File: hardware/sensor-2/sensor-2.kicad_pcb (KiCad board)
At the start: 2 copper layers, 11 x 155 mm, 16 parts, among them J101 2x05_Horizontal, U101 A31010SEHALT-10, U102 A31010SEHALT-10, U103 A31010SEHALT-10

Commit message: Update sensors
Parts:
- C101, C103, C104: footprint Capacitor_SMD:C_0603_1608Metric -> V2_Capacitor_SMD:C_0603
- FID101, FID102: value Fiducial -> Fiducial_Paste
- INFO101: value ORDER-NUMBER -> Order_Number

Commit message: Replace Order_Number
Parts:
- H107, H108: value MountingHole_2.5mm -> 2.5mm
- INFO101: value Order_Number -> ~; footprint V2_Production:Order_Number -> V2_Production:Revision
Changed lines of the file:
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@@
 	(paper "A4")
 	(title_block
-		(date "2023-07-17")
-		(rev "1")
+		(date "2026-02-13")
+		(rev "2026-02-13")
 	)
 	(layers
@@
 			)
 		)
+		(pad "" smd roundrect
+			(at -0.7 0)
+			(size 0.7 0.8)
+			(layers "F.Paste")
+			(roundrect_rratio 0.1428571429)
+			(chamfer_ratio 0.3)
+			(chamfer top_right bottom_right)
+		)
+		(pad "" smd roundrect
+			(at 0.7 0)
+			(size 0.7 0.8)
+			(layers "F.Paste")
+			(roundrect_rratio 0.1428571429)
+			(chamfer_ratio 0.3)
+			(chamfer top_left bottom_left)
+		)
 		(pad "1" smd roundrect
 			(at -0.7 0)
 			(size 0.7 0.8)
-			(layers "F.Cu" "F.Mask" "F.Paste")
+			(layers "F.Cu" "F.Mask")
 			(roundrect_rratio 0.1428571429)
 			(net 1 "+3V3")
@@
 			(at 0.7 0)
 			(size 0.7 0.8)
-			(layers "F.Cu" "F.Mask" "F.Paste")
+			(layers "F.Cu" "F.Mask")
 			(roundrect_rratio 0.1428571429)
 			(net 4 "GND")
@@
 		)
 		(embedded_fonts no)
-		(model "${KICAD9_3DMODEL_DIR}/Capacitor_SMD.3dshapes/C_0603_1608Metric.step"
+		(model "../../3dmodels/V2_Capacitor_SMD.3dshapes/C_0603_1608Metric.step"
 			(offset
 				(xyz 0 0 0)
@@
 		)
 		(embedded_fonts no)
-		(model "/Users/kay/Documents/KiCad/8.0/versioduo.kicad/3dmodels/V2_Sensor_Hall.3dshapes/A31010SEHALT-10.stp"
+		(model "../../3dmodels/V2_Sensor_Hall.3dshapes/A31010SEHALT-10.stp"
 			(offset
 				(xyz 0 0 0)
@@
 			)
 		)
-		(property "Value" "MountingHole_2.5mm"
+		(property "Value" "2.5mm"
 			(at 0 2.23 0)
 			(unlocked yes)
@@
 			)
 		)
+		(pad "" smd roundrect
+			(at -0.7 0)
+			(size 0.7 0.8)
+			(layers "F.Paste")
+			(roundrect_rratio 0.1428571429)
+			(chamfer_ratio 0.3)
+			(chamfer top_right bottom_right)
+		)
+		(pad "" smd roundrect
+			(at 0.7 0)
+			(size 0.7 0.8)
+			(layers "F.Paste")
+			(roundrect_rratio 0.1428571429)
+			(chamfer_ratio 0.3)
+			(chamfer top_left bottom_left)
+		)
 		(pad "1" smd roundrect
 			(at -0.7 0)
 			(size 0.7 0.8)
-			(layers "F.Cu" "F.Mask" "F.Paste")
+			(layers "F.Cu" "F.Mask")
 			(roundrect_rratio 0.1428571429)
 			(net 1 "+3V3")
@@
 			(at 0.7 0)
 			(size 0.7 0.8)
-			(layers "F.Cu" "F.Mask" "F.Paste")
+			(layers "F.Cu" "F.Mask")
 			(roundrect_rratio 0.1428571429)
 			(net 4 "GND")
@@
 		)
 		(embedded_fonts no)
-		(model "${KICAD9_3DMODEL_DIR}/Capacitor_SMD.3dshapes/C_0603_1608Metric.step"
+		(model "../../3dmodels/V2_Capacitor_SMD.3dshapes/C_0603_1608Metric.step"
 			(offset
 				(xyz 0 0 0)
@@
 		)
 		(embedded_fonts no)
-		(model "/Users/kay/Documents/KiCad/8.0/versioduo.kicad/3dmodels/V2_Sensor_Hall.3dshapes/A31010SEHALT-10.stp"
+		(model "../../3dmodels/V2_Sensor_Hall.3dshapes/A31010SEHALT-10.stp"
 			(offset
 				(xyz 0 0 0)
@@
 		)
 	)
-	(footprint "V2_Production:Order_Number"
+	(footprint "V2_Production:Revision"
 		(layer "F.Cu")
 		(at 159.75 78.25 90)
@@
 			)
 		)
-		(property "Value" "Order_Number"
+		(property "Value" "~"
 			(at 0 2.27 90)
 			(unlocked yes)
@@
 		(sheetname "/")
 		(sheetfile "sensor-2.kicad_sch")
-		(attr exclude_from_pos_files exclude_from_bom)
-		(fp_rect
-			(start -7 -0.75)
-			(end 7 0.75)
-			(stroke
-				(width 0.05)
-				(type default)
-			)
-			(fill no)
-			(layer "F.CrtYd")
-		)
-		(fp_text user "${Order-Number}"
+		(attr exclude_from_pos_files exclude_from_bom allow_missing_courtyard)
+		(fp_text user "${REVISION} (${ISSUE_DATE})"
 			(at 0 0 90)
 			(unlocked yes)
@@
 			(effects
 				(font
-					(size 0.8 0.8)
-					(thickness 0.12)
+					(size 0.75 0.75)
+					(thickness 0.1)
+				)
+			)
+		)
+		(fp_text user "${REVISION} (${ISSUE_DATE})"
+			(at 0 0 90)
+			(unlocked yes)
+			(layer "F.Fab")
+			(effects
+				(font
+					(size 0.75 0.75)
+					(thickness 0.1)
 				)
 			)
@@
 		)
 		(embedded_fonts no)
-		(model "/Users/kay/Documents/KiCad/8.0/versioduo.kicad/3dmodels/V2_Sensor_Hall.3dshapes/A31010SEHALT-10.stp"
+		(model "../../3dmodels/V2_Sensor_Hall.3dshapes/A31010SEHALT-10.stp"
 			(offset
 				(xyz 0 0 0)
@@
 			)
 		)
-		(property "Value" "MountingHole_2.5mm"
+		(property "Value" "2.5mm"
 			(at 0 2.23 0)
 			(unlocked yes)
@@
 			)
 		)
+		(pad "" smd roundrect
+			(at -0.7 0)
+			(size 0.7 0.8)
+			(layers "F.Paste")
+			(roundrect_rratio 0.1428571429)
+			(chamfer_ratio 0.3)
+			(chamfer top_right bottom_right)
+		)
+		(pad "" smd roundrect
+			(at 0.7 0)
+			(size 0.7 0.8)
+			(layers "F.Paste")
+			(roundrect_rratio 0.1428571429)
+			(chamfer_ratio 0.3)
+			(chamfer top_left bottom_left)
+		)
 		(pad "1" smd roundrect
 			(at -0.7 0)
 			(size 0.7 0.8)
-			(layers "F.Cu" "F.Mask" "F.Paste")
+			(layers "F.Cu" "F.Mask")
 			(roundrect_rratio 0.1428571429)
 			(net 1 "+3V3")
@@
 			(at 0.7 0)
 			(size 0.7 0.8)
-			(layers "F.Cu" "F.Mask" "F.Paste")
+			(layers "F.Cu" "F.Mask")
 			(roundrect_rratio 0.1428571429)
 			(net 4 "GND")
@@
 		)
 		(embedded_fonts no)
-		(model "${KICAD9_3DMODEL_DIR}/Capacitor_SMD.3dshapes/C_0603_1608Metric.step"
+		(model "../../3dmodels/V2_Capacitor_SMD.3dshapes/C_0603_1608Metric.step"
 			(offset
 				(xyz 0 0 0)

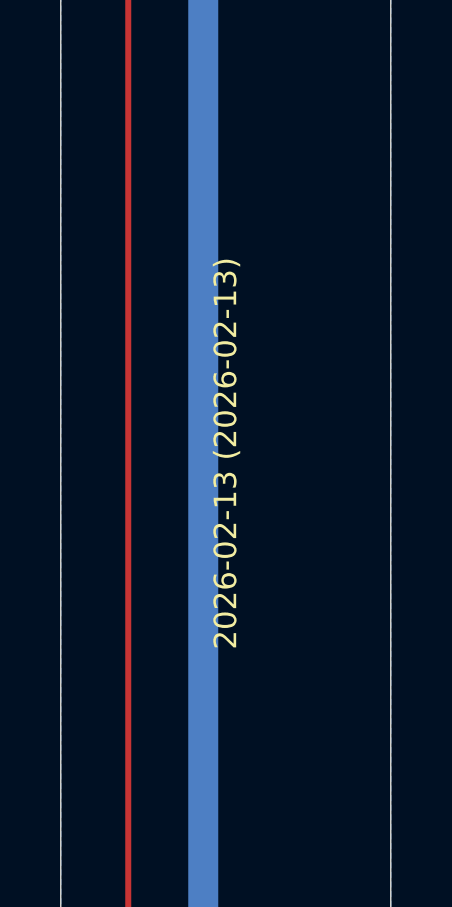
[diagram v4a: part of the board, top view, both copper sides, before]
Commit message: KiCad 10
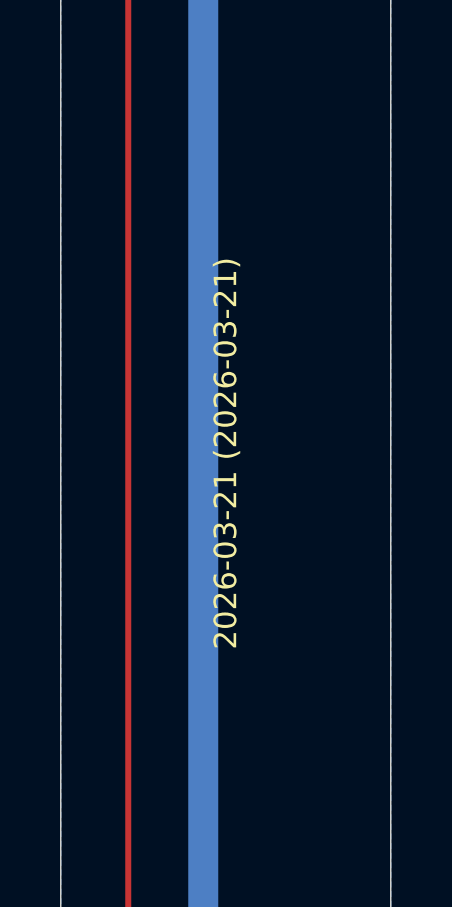
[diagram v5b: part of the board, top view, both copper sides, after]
